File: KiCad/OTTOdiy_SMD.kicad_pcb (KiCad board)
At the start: 4 copper layers, 297 x 91 mm, 424 parts, among them CN201 1x4 MALE Molex PicoBlade, CN202 1x4 MALE Molex PicoBlade, J1 Conn_ARM_JTAG_SWD_10, J2 Conn_02x04, J201 Raspberry Pi Connector, J202 Conn_02x04, J203 Conn_02x05, J204 Conn_02x05, J205 Conn_02x04, J206 Conn_02x06, J207 Conn_02x03, Q1 AO4485, SW1 ALPS SKHH OR SKPF, SW10 ALPS SKHH OR SKPF, SW11 ALPS SKHH OR SKPF, SW12 ALPS SKHH OR SKPF, SW13 ALPS SKHH OR SKPF, SW14 ALPS SKHH OR SKPF, SW15 ALPS SKHH OR SKPF, SW16 ALPS SKHH OR SKPF, SW17 ALPS SKHH OR SKPF, SW18 ALPS SKHH OR SKPF, SW19 ALPS SKHH OR SKPF, SW2 ALPS SKHH OR SKPF, SW20 ALPS SKHH OR SKPF, SW201 6x6x5mm, SW202 SW_DIP_x02, SW203 6x6x5.85mm (RA), SW21 ALPS SKHH OR SKPF, SW22 ALPS SKHH OR SKPF, SW23 ALPS SKHH OR SKPF, SW24 ALPS SKHH OR SKPF, SW25 ALPS SKHH OR SKPF, SW26 ALPS SKHH OR SKPF, SW27 6x6x13mm, SW28 6x6x13mm, SW29 6x6x13mm, SW3 ALPS SKHH OR SKPF, SW30 6x6x13mm, SW31 6x6x13mm, SW32 6x6x13mm, SW33 6x6x13mm, SW34 6x6x13mm, SW35 6x6x13mm, SW36 6x6x13mm, SW37 6x6x13mm, SW38 6x6x13mm, SW39 6x6x13mm, SW4 ALPS SKHH OR SKPF, SW40 6x6x13mm, SW41 6x6x13mm, SW42 6x6x13mm, SW43 6x6x13mm, SW44 6x6x13mm, SW45 6x6x13mm, SW46 6x6x13mm, SW47 6x6x13mm, SW48 SW_DIP_x02, SW49 SW_SP3T (DP3T Parallel), SW5 ALPS SKHH OR SKPF, SW6 ALPS SKHH OR SKPF, SW7 ALPS SKHH OR SKPF, SW8 ALPS SKHH OR SKPF, SW9 ALPS SKHH OR SKPF, U1 SN74LV1T125_SOT-23_A, U2 TPS22918_SOT23-6_A, U202 STM32F407VGTx, U204 USB6B1, U205 SN74HC14, U206 H11L1S, U207 WM8731, U208 TPS79533, U3 LTC3112_TSSOP20_A, U4 TLV62568_SOT-23-5_A, U5 TPS22918_SOT23-6_A, Y201 25MHz, Y202 32.768kHz, Y203 12.288MHz

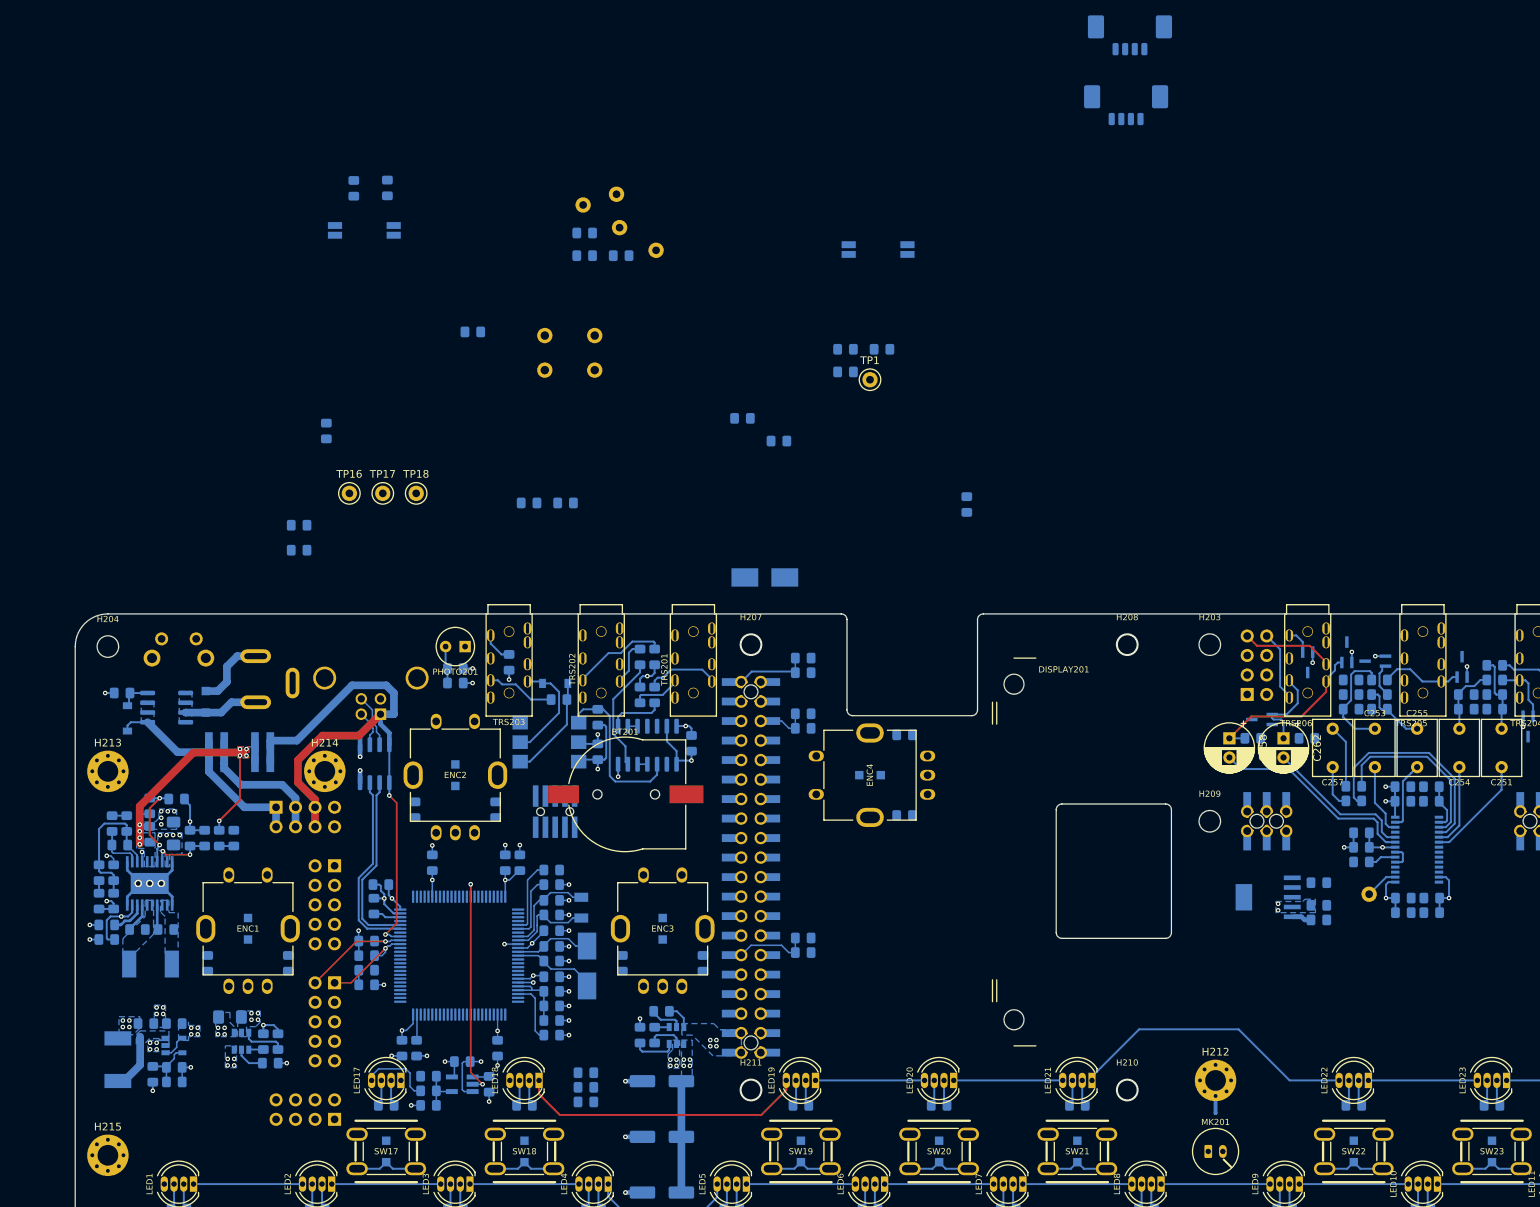
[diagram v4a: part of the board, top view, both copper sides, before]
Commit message: Placement of all components
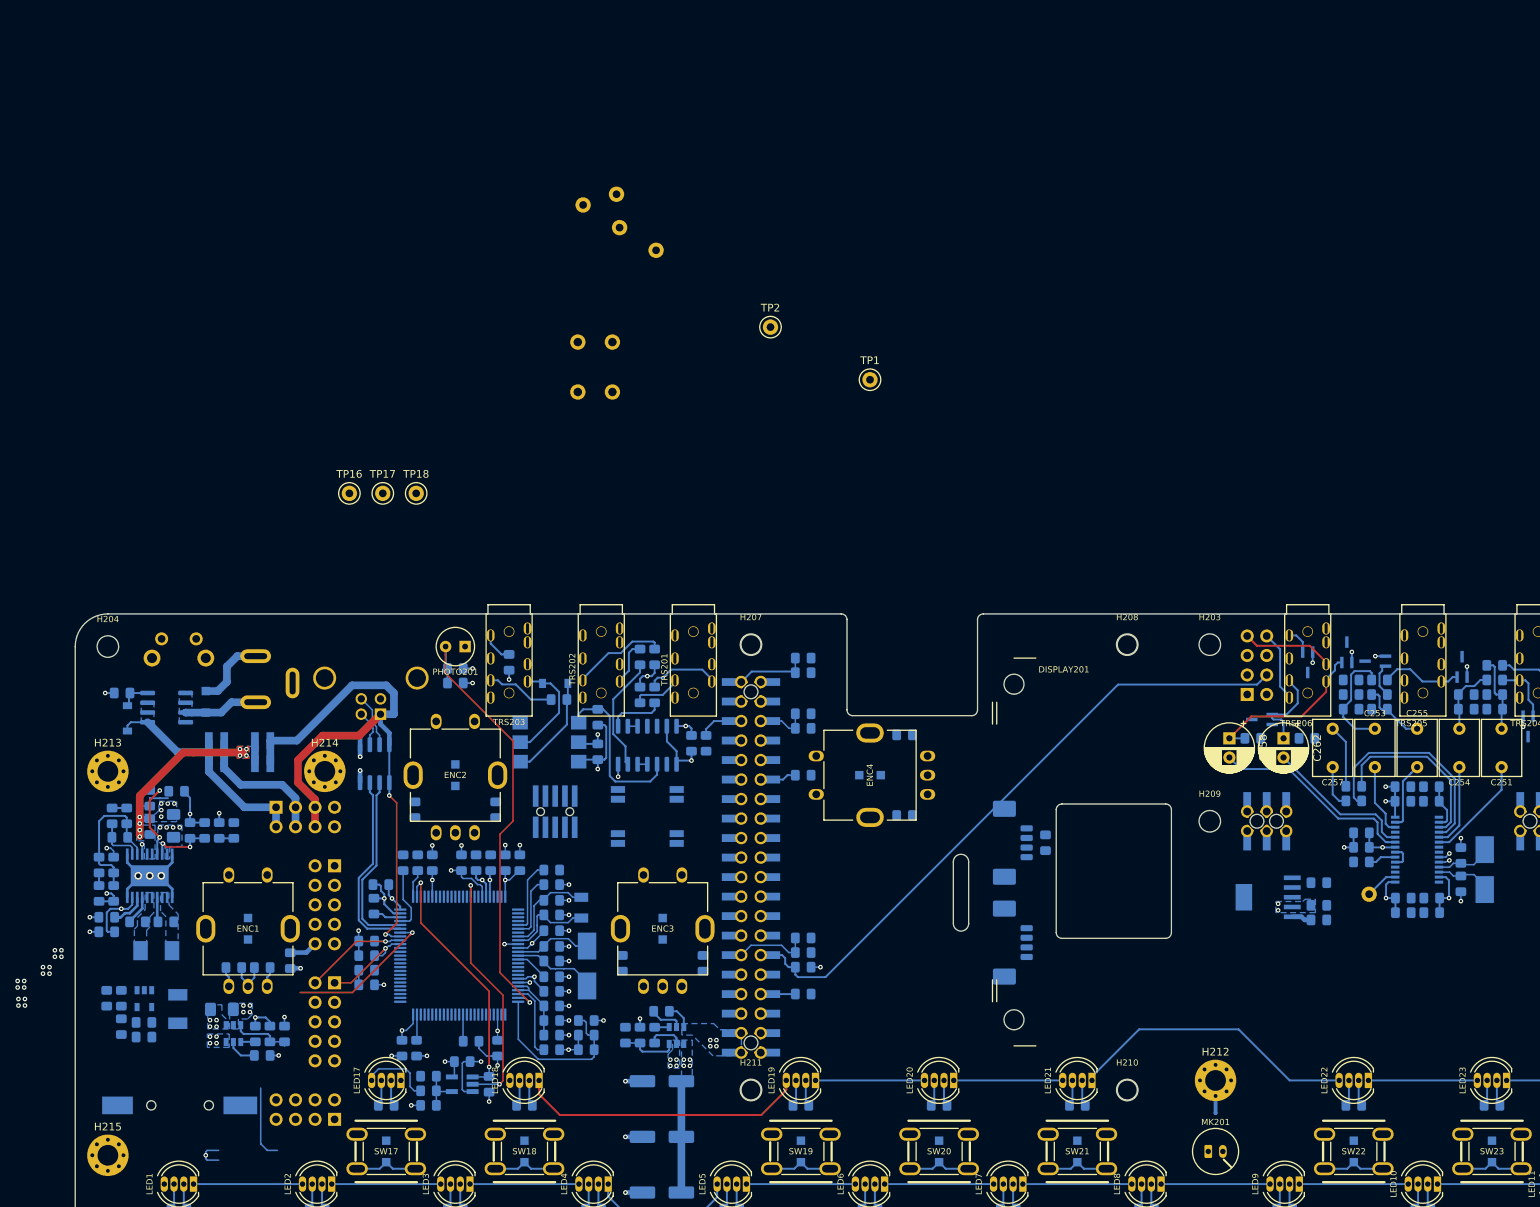
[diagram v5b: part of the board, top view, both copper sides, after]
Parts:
- added TP2: TestPoint, TestPoint:TestPoint_Keystone_5000-5004_Miniature, F.Cu at (131.0, 68.2)
- BT201: moved to B.Cu
- L1: footprint OTTO_Footprints_Lib:L_7.3x6.6_H3 -> OTTO_Footprints_Lib:L_5.75x5.2_H3
- L2: footprint OTTO_Footprints_Lib:L_7.3x6.6_H3 -> OTTO_Footprints_Lib:L_4.75x4.2_H2
- R6, R7: value 47k -> 10k
- moved CN202 119.8 mm to (162.0, 148.3), turned to 90 degrees
- moved R204 111.7 mm to (92.0, 161.2), turned to 180 degrees
- moved C265 109.5 mm to (220.9, 136.9), turned to 90 degrees
- moved C266 105.9 mm to (220.9, 140.7), turned to 270 degrees
- moved R3 103.1 mm to (135.3, 155.0), turned to 180 degrees
- moved Y203 101.2 mm to (224.1, 138.8), turned to 270 degrees
- moved CN201 97.9 mm to (162.0, 135.3), turned to 90 degrees
- moved R26 93.2 mm to (135.3, 151.5)
- moved R4 92.3 mm to (102.5, 152.8), turned to 180 degrees
- moved R203 88.9 mm to (90.8, 137.9)
- moved R6 88.3 mm to (83.2, 137.9), turned to 270 degrees
- moved R7 84.8 mm to (85.1, 137.9), turned to 90 degrees
- moved SW48 82.4 mm to (115.0, 134.8), turned to 180 degrees
- moved SW202 82.2 mm to (115.0, 129.0)
- moved R32 78.2 mm to (67.8, 160.2), turned to 90 degrees
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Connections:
- J201 pad 26: Net-(J201-Pad26) -> /CE1_GPIO7_RASPI
- SW202 pad 1: /MCU/BOOT0 -> +3V3_MCU
- SW202 pad 2: /MCU/BOOT1 -> +3V3_MCU
- SW202 pad 3: +3V3_MCU -> /MCU/BOOT1
- SW202 pad 4: +3V3_MCU -> /MCU/BOOT0
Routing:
- net AMP_ENABLE: track 0.00 -> 82.9 mm
- net /MCU/BRIGHTNESS: track 4.85 -> 58.9 mm, vias 0 -> 1
- net /MCU/SPI_CS_MCU_LED: track 2.18 -> 33.1 mm, vias 0 -> 2
- net /MCU/3V3_RASPI_DIV_2: track 0.00 -> 22.5 mm
- net /MCU/LED_PWR_EN: track 0.00 -> 20.6 mm, vias 0 -> 2
- net GND: track 301.2 -> 318.1 mm, vias 72 -> 76
- net Net-(R10-Pad1): track 5.61 -> 17.9 mm
- net /MCU/DC_IN: track 38.5 -> 28.7 mm
- net /ICP_SWDIO: track 0.00 -> 8.32 mm
- net /MCU/PERIPHERALS/3V3_SW: track 7.46 -> 0.00 mm
- net +3V3_MCU: track 35.4 -> 42.8 mm, vias 15 -> 16
- net Net-(C266-Pad1): track 0.00 -> 7.36 mm
- net Net-(C265-Pad1): track 0.00 -> 7.36 mm
- net Net-(C93-Pad2): track 6.95 -> 0.00 mm
- net /MCU/BOOT0: track 0.00 -> 6.73 mm, vias 0 -> 1
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- removed copper zone on B.Cu, net +3V3_MCU
- removed copper zone on B.Cu, net /MCU/PERIPHERALS/3V3_SW
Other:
- outline, holes or cut-outs redrawn

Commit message: change mcu reset button and route more stuff
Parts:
- SW201: value 6x6x5mm -> 5.2x5.2x1.5mm; footprint Button_Switch_THT:SW_PUSH_6mm_H5mm -> OTTO_Footprints_Lib:SW_SPST_5.2x5.2x1.5mm
- TP6, TP7, TP8, TP9: moved to F.Cu
- moved TP1 105.6 mm to (78.5, 157.8)
- moved SW201 96.9 mm to (107.0, 167.0), turned to 180 degrees
- moved TP8 85.1 mm to (134.0, 137.2)
- moved TP6 84.5 mm to (134.0, 132.2)
- moved TP9 76.1 mm to (134.0, 123.3)
- moved TP7 69.3 mm to (123.0, 127.1)
- moved TP2 64.5 mm to (123.0, 132.2)
- moved TP17 60.8 mm to (109.3, 143.4)
- moved TP16 59.8 mm to (109.3, 139.5)
- moved TP18 52.0 mm to (106.8, 137.0)
- moved C48 43.3 mm to (97.4, 162.1), turned to 90 degrees
- moved R19 2.85 mm to (45.6, 156.6), turned to 180 degrees
- moved C93 1.80 mm to (44.6, 153.8)
- moved R18 1.80 mm to (46.5, 153.8)
- moved R204 1.37 mm to (90.9, 161.9)
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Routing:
- net AMP_ENABLE: track 82.9 -> 24.0 mm
- net SPI_MOSI_RASPI: track 0.00 -> 46.1 mm
- net SPI_CS_RASPI_DISPLAY: track 0.00 -> 43.4 mm
- net BL_PWM: track 0.00 -> 42.5 mm
- net SPI_SCLK_RASPI: track 0.00 -> 38.5 mm
- net /ICP_RST: track 4.33 -> 33.1 mm
- net GND: track 318.1 -> 335.1 mm, vias 76 -> 82
- net Net-(R10-Pad1): track 17.9 -> 8.09 mm
- net +3V3_RASPI: track 32.0 -> 40.4 mm, vias 6 -> 7
- net /GPIO1_RASPI: track 0.00 -> 6.16 mm
- net Net-(C93-Pad2): track 0.00 -> 5.71 mm
- net /GPIO0_RASPI: track 0.00 -> 4.81 mm
- net +5V_RASPI: track 3.40 -> 7.15 mm
- net /PWM1_GPIO13_RASPI: track 0.00 -> 3.32 mm
- net /CE1_GPIO7_RASPI: track 0.00 -> 2.79 mm
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- added copper zone on B.Cu, net +3V3_MCU
- added copper zone on B.Cu, net /MCU/PERIPHERALS/3V3_SW
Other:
- outline, holes or cut-outs redrawn
- board text added: "MCU RESET"

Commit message: add analog ground layout
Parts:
- added FID1: Fiducial, Fiducial:Fiducial_1mm_Mask2mm, F.Cu at (188.8, 86.5)
- added FID10: Fiducial, Fiducial:Fiducial_1mm_Mask2mm, B.Cu at (208.3, 85.2)
- added FID11: Fiducial, Fiducial:Fiducial_1mm_Mask2mm, B.Cu at (211.9, 88.7)
- added FID12: Fiducial, Fiducial:Fiducial_1mm_Mask2mm, B.Cu at (215.4, 92.2)
- added FID2: Fiducial, Fiducial:Fiducial_1mm_Mask2mm, F.Cu at (188.8, 90.0)
- added FID3: Fiducial, Fiducial:Fiducial_1mm_Mask2mm, F.Cu at (192.3, 86.5)
- added FID4: Fiducial, Fiducial:Fiducial_1mm_Mask2mm, F.Cu at (188.8, 93.6)
- added FID5: Fiducial, Fiducial:Fiducial_1mm_Mask2mm, F.Cu at (192.3, 90.0)
- added FID6: Fiducial, Fiducial:Fiducial_1mm_Mask2mm, F.Cu at (195.8, 86.5)
- added FID7: Fiducial, Fiducial:Fiducial_1mm_Mask2mm, B.Cu at (204.8, 85.2)
- added FID8: Fiducial, Fiducial:Fiducial_1mm_Mask2mm, B.Cu at (208.3, 88.7)
- added FID9: Fiducial, Fiducial:Fiducial_1mm_Mask2mm, B.Cu at (211.9, 92.2)
- added NT1: Net-Tie_2, OTTO_Footprints_Lib:NetTie-2_Pad5.0mm, B.Cu at (191.1, 140.1)
- moved C267 4.00 mm to (202.4, 144.5)
- moved C268 4.00 mm to (202.4, 147.4)
- moved C75 4.00 mm to (202.4, 149.3)
- moved U208 4.00 mm to (195.8, 146.4)
- moved C232 0.95 mm to (166.3, 133.5)
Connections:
- C246 pad 1: GND -> GNDA
- C250 pad 1: GND -> GNDA
- C252 pad 2: GND -> GNDA
- C256 pad 2: GND -> GNDA
- C259 pad 2: GND -> GNDA
- C264 pad 1: GND -> GNDA
- C267 pad 1: GND -> GNDA
- C268 pad 1: GND -> GNDA
- C72 pad 2: GND -> GNDA
- C73 pad 2: GND -> GNDA
- C74 pad 2: GND -> GNDA
- C75 pad 2: GND -> GNDA
- D50 pad 1: GND -> GNDA
- D51 pad 1: GND -> GNDA
- D52 pad 1: GND -> GNDA
- D53 pad 1: GND -> GNDA
- D54 pad 2: GND -> GNDA
- D55 pad 2: GND -> GNDA
- D56 pad 1: GND -> GNDA
- J2 pad 5: GND -> GNDA
- J2 pad 6: GND -> GNDA
- MK201 pad 1: GND -> GNDA
- R219 pad 2: GND -> GNDA
- R221 pad 1: GND -> GNDA
- R224 pad 2: GND -> GNDA
- R225 pad 1: GND -> GNDA
- R228 pad 1: GND -> GNDA
- R229 pad 1: GND -> GNDA
- R230 pad 1: GND -> GNDA
- R26 pad 2: GND -> GNDA
- TRS204 pad R2: GND -> GNDA
- TRS204 pad S: GND -> GNDA
- TRS205 pad R2: GND -> GNDA
- TRS205 pad S: GND -> GNDA
- TRS206 pad R2: GND -> GNDA
- U207 pad 11: GND -> GNDA
- U207 pad 15: GND -> GNDA
- U208 pad 3: GND -> GNDA
- U208 pad 6: GND -> GNDA
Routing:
- net AMP_ENABLE: track 24.0 -> 4.14 mm
- net GNDA: track 0.00 -> 17.7 mm, vias 0 -> 21
- net Net-(R227-Pad1): track 28.8 -> 11.8 mm, vias 0 -> 2
- net Net-(R226-Pad1): track 23.3 -> 15.5 mm, vias 0 -> 2
- net GND: track 335.1 -> 337.9 mm, vias 82 -> 81
- net /AUDIO/HP_OUT_R: track 11.7 -> 13.7 mm
- net SPI_MOSI_RASPI: track 46.1 -> 44.7 mm
- net +3V3_RASPI: track 40.4 -> 39.4 mm
- added copper zone on B.Cu, net GNDA
- added copper zone on F.Cu, net GNDA
- added copper zone on In2.Cu, net GNDA
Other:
- outline, holes or cut-outs redrawn

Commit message: misc raspi routing
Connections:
- J201 pad 13: LO_SENSE -> LI_SENSE
- J201 pad 22: HP_SENSE -> LO_SENSE
- J201 pad 37: LI_SENSE -> HP_SENSE
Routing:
- net I2C_SDA: track 4.99 -> 203.5 mm
- net I2C_SCL: track 5.65 -> 200.0 mm
- net I2S_DIN: track 0.00 -> 128.7 mm
- net LI_SENSE: track 0.00 -> 126.3 mm
- net LO_SENSE: track 0.00 -> 109.6 mm
- net HP_SENSE: track 0.00 -> 88.3 mm
- net /AUDIO/I2S_LRCLK*: track 3.10 -> 89.1 mm
- net /MCU/COL_5: track 0.00 -> 52.0 mm
- net /MCU/COL_6: track 0.00 -> 45.5 mm
- net MIDI_OUT: track 0.00 -> 40.0 mm, vias 0 -> 1
- net /MCU/COL_4: track 0.00 -> 39.0 mm
- net MIDI_IN: track 21.8 -> 52.0 mm, vias 0 -> 1
- net GND: track 337.9 -> 345.8 mm, vias 81 -> 87
- net Net-(D33-Pad2): track 0.00 -> 7.79 mm
- net Net-(D32-Pad2): track 0.00 -> 7.79 mm
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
